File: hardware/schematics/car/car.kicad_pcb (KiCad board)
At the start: 12 copper layers, 17.9 x 30.1 mm, 19 parts, among them M1 Motor_Servo, Q1 PMOS, SW2 SW_Push, SW3 SW_Push, U1 VL53L0CXV0DH1, U10 Mini-560, U11 JGA25-37x, U2 VL53L0CXV0DH1, U3 VL53L0CXV0DH1, U4 Pixy2, U6 TB6612FNG, U7 SparkFun OTOS, U9 Mini-360

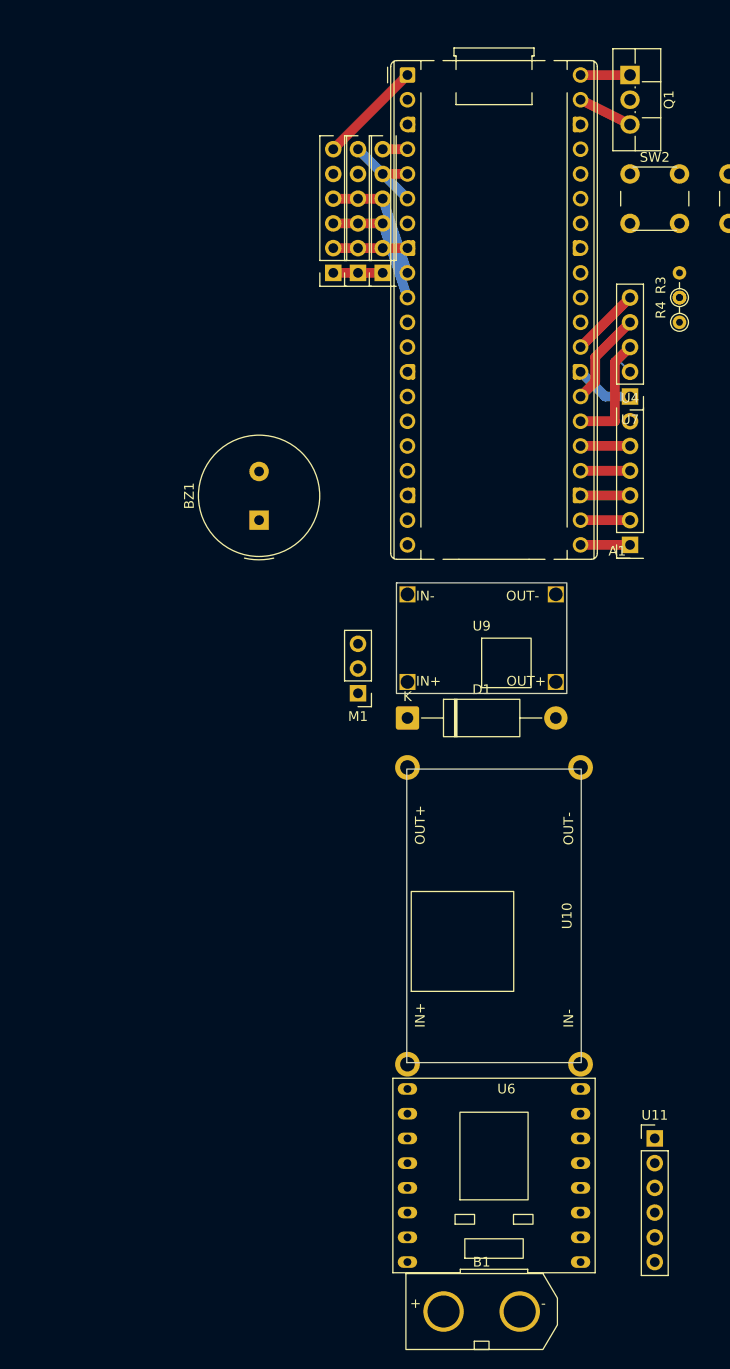
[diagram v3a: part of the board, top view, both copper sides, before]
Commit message: [Schematic] Fix mini560 footprint. PCB: some moving.
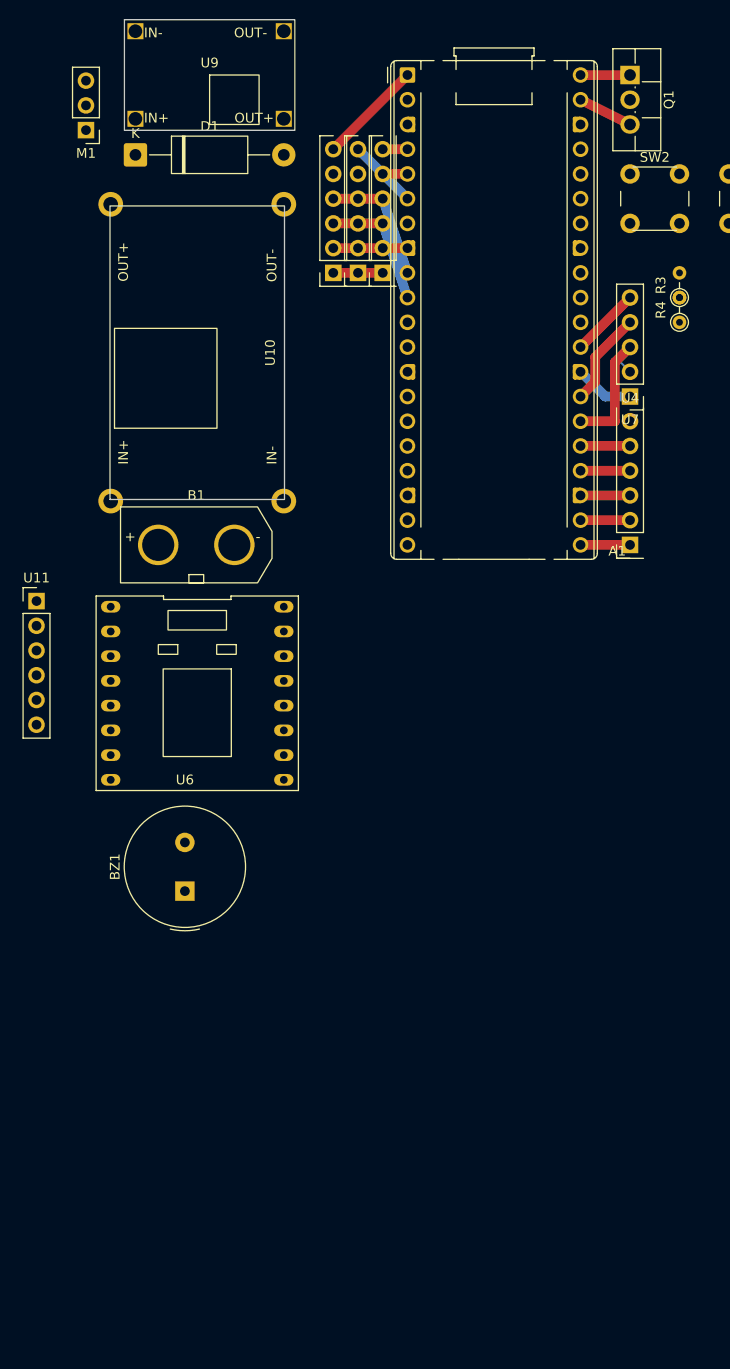
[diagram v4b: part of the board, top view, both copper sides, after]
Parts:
- moved U11 84.1 mm to (88.9, 69.3)
- moved B1 84.0 mm to (105.3, 63.5)
- moved U10 65.4 mm to (105.4, 43.8)
- moved D1 64.2 mm to (99.1, 23.4)
- moved M1 64.2 mm to (94.0, 20.9)
- moved U9 64.2 mm to (106.7, 15.2)
- moved U6 58.2 mm to (105.4, 78.7), turned to -90 degrees
- moved BZ1 38.9 mm to (104.1, 99.1)
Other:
- board size 17.9 x 30.1 mm -> 17.9 x 30.2 mm
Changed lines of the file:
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@@
 	(footprint "xlnc-foot:Buck_Mini-560_2.54mm"
 		(layer "F.Cu")
-		(at 135.89 101.6 90)
+		(at 105.41 43.76 90)
 		(property "Reference" "U10"
 			(at 0 7.5 90)
@@
 		(sheetname "/")
 		(sheetfile "car.kicad_sch")
-		(units
-			(unit
-				(name "A")
-				(pins "1" "2" "3" "4")
-			)
-		)
 		(attr smd)
 		(duplicate_pad_numbers_are_jumpers no)
@@
 		)
 		(pad "3" thru_hole circle
-			(at 15.24 -8.89 90)
+			(at 15.24 8.89 90)
 			(size 2.54 2.54)
 			(drill 1.5)
@@
 		)
 		(pad "4" thru_hole circle
-			(at 15.24 8.89 90)
+			(at 15.24 -8.89 90)
 			(size 2.54 2.54)
 			(drill 1.5)
@@
 	(footprint "xlnc-foot:TB6612FNG_Breakout_Sparkfun"
 		(layer "F.Cu")
-		(at 135.89 128.27 90)
+		(at 105.41 78.74 -90)
 		(tags "TB6612FNG, driver motor")
 		(property "Reference" "U6"
@@
 		(duplicate_pad_numbers_are_jumpers no)
 		(fp_line
-			(start 9.99 -10.39)
-			(end -9.99 -10.39)
+			(start -9.99 10.39)
+			(end 9.99 10.39)
 			(stroke
 				(width 0.12)
@@
 		)
 		(fp_line
-			(start -9.99 -10.39)
-			(end -9.99 -3.463333)
+			(start 9.99 10.39)
+			(end 9.99 -10.39)
 			(stroke
 				(width 0.12)
@@
 		)
 		(fp_line
-			(start -9.63 -3.463333)
-			(end -9.63 3.463333)
+			(start -9.99 3.463333)
+			(end -9.99 10.39)
 			(stroke
 				(width 0.12)
@@
 		)
 		(fp_line
-			(start -9.99 -3.463333)
-			(end -9.63 -3.463333)
+			(start -9.63 3.463333)
+			(end -9.99 3.463333)
 			(stroke
 				(width 0.12)
@@
 		)
 		(fp_line
-			(start -9.63 3.463333)
-			(end -9.99 3.463333)
+			(start -9.99 -3.463333)
+			(end -9.63 -3.463333)
 			(stroke
 				(width 0.12)
@@
 		)
 		(fp_line
-			(start -9.99 3.463333)
-			(end -9.99 10.39)
+			(start -9.63 -3.463333)
+			(end -9.63 3.463333)
 			(stroke
 				(width 0.12)
@@
 		)
 		(fp_line
-			(start 9.99 10.39)
-			(end 9.99 -10.39)
+			(start -9.99 -10.39)
+			(end -9.99 -3.463333)
 			(stroke
 				(width 0.12)
@@
 		)
 		(fp_line
-			(start -9.99 10.39)
-			(end 9.99 10.39)
+			(start 9.99 -10.39)
+			(end -9.99 -10.39)
 			(stroke
 				(width 0.12)
@@
 		)
 		(fp_rect
-			(start -5 -4)
-			(end -4 -2)
+			(start -5 2)
+			(end -4 4)
 			(stroke
 				(width 0.1)
@@
 		)
 		(fp_rect
-			(start -2.5 -3.5)
-			(end 6.5 3.5)
+			(start -8.5 -3)
+			(end -6.5 3)
 			(stroke
 				(width 0.1)
@@
 		)
 		(fp_rect
-			(start -8.5 -3)
-			(end -6.5 3)
+			(start -2.5 -3.5)
+			(end 6.5 3.5)
 			(stroke
 				(width 0.1)
@@
 		)
 		(fp_rect
-			(start -5 2)
-			(end -4 4)
+			(start -5 -4)
+			(end -4 -2)
 			(stroke
 				(width 0.1)
@@
 		)
 		(fp_line
-			(start 9.74 -10.14)
-			(end 9.74 10.14)
+			(start -9.74 10.14)
+			(end -9.74 -10.14)
 			(stroke
 				(width 0.05)
@@
 		)
 		(fp_line
-			(start -9.74 -10.14)
-			(end 9.74 -10.14)
+			(start 9.74 10.14)
+			(end -9.74 10.14)
 			(stroke
 				(width 0.05)
@@
 		)
 		(fp_line
-			(start 9.74 10.14)
-			(end -9.74 10.14)
+			(start -9.74 -10.14)
+			(end 9.74 -10.14)
 			(stroke
 				(width 0.05)
@@
 		)
 		(fp_line
-			(start -9.74 10.14)
-			(end -9.74 -10.14)
+			(start 9.74 -10.14)
+			(end 9.74 10.14)
 			(stroke
 				(width 0.05)
@@
 		)
 		(pad "1" thru_hole oval
-			(at -1.27 8.89 90)
+			(at -1.27 8.89 270)
 			(size 1.2 2)
 			(drill 0.8)
@@
 		)
 		(pad "5" thru_hole oval
-			(at 1.27 8.89 90)
+			(at 1.27 8.89 270)
 			(size 1.2 2)
 			(drill 0.8)
@@
 		)
 		(pad "7" thru_hole oval
-			(at 3.81 8.89 90)
+			(at 3.81 8.89 270)
 			(size 1.2 2)
 			(drill 0.8)
@@
 		)
 		(pad "11" thru_hole oval
-			(at 6.35 8.89 90)
+			(at 6.35 8.89 270)
 			(size 1.2 2)
 			(drill 0.8)
@@
 		)
 		(pad "15" thru_hole oval
-			(at 6.35 -8.89 90)
+			(at 6.35 -8.89 270)
 			(size 1.2 2)
 			(drill 0.8)
@@
 		)
 		(pad "16" thru_hole oval
-			(at 3.81 -8.89 90)
+			(at 3.81 -8.89 270)
 			(size 1.2 2)
 			(drill 0.8)
@@
 		)
 		(pad "17" thru_hole oval
-			(at 1.27 -8.89 90)
+			(at 1.27 -8.89 270)
 			(size 1.2 2)
 			(drill 0.8)
@@
 		)
 		(pad "18" thru_hole oval
-			(at -3.81 8.89 90)
+			(at -3.81 8.89 270)
 			(size 1.2 2)
 			(drill 0.8)
@@
 		)
 		(pad "18" thru_hole oval
-			(at 8.89 -8.89 90)
+			(at 8.89 -8.89 270)
 			(size 1.2 2)
 			(drill 0.8)
@@
 		)
 		(pad "18" thru_hole oval
-			(at 8.89 8.89 90)
+			(at 8.89 8.89 270)
 			(size 1.2 2)
 			(drill 0.8)
@@
 		)
 		(pad "19" thru_hole oval
-			(at -1.27 -8.89 90)
+			(at -1.27 -8.89 270)
 			(size 1.2 2)
 			(drill 0.8)
@@
 		)
 		(pad "20" thru_hole oval
-			(at -6.35 8.89 90)
+			(at -6.35 8.89 270)
 			(size 1.2 2)
 			(drill 0.8)
@@
 		)
 		(pad "21" thru_hole oval
-			(at -3.81 -8.89 90)
+			(at -3.81 -8.89 270)
 			(size 1.2 2)
 			(drill 0.8)
@@
 		)
 		(pad "22" thru_hole oval
-			(at -6.35 -8.89 90)
+			(at -6.35 -8.89 270)
 			(size 1.2 2)
 			(drill 0.8)
@@
 		)
 		(pad "23" thru_hole oval
-			(at -8.89 -8.89 90)
+			(at -8.89 -8.89 270)
 			(size 1.2 2)
 			(drill 0.8)
@@
 		)
 		(pad "24" thru_hole oval
-			(at -8.89 8.89 90)
+			(at -8.89 8.89 270)
 			(size 1.2 2)
 			(drill 0.8)
@@
 	(footprint "xlnc-foot:Buck_Mini-360"
 		(layer "F.Cu")
-		(at 134.62 73.08)
+		(at 106.68 15.24)
 		(property "Reference" "U9"
 			(at 0 -1.25 0)
@@
 	(footprint "Diode_THT:D_DO-15_P15.24mm_Horizontal"
 		(layer "F.Cu")
-		(at 127 81.28)
+		(at 99.06 23.44)
 		(descr "Diode, DO-15 series, Axial, Horizontal, pin pitch=15.24mm, length*diameter=7.6*3.6mm^2, http://www.diodes.com/_files/packages/DO-15.pdf")
 		(tags "Diode DO-15 series Axial Horizontal pin pitch 15.24mm  length 7.6mm diameter 3.6mm")
@@
 	(footprint "xlnc-foot:XT60"
 		(layer "F.Cu")
-		(at 134.62 142.24)
+		(at 105.31 63.5)
 		(property "Reference" "B1"
 			(at 0 -5.08 0)
@@
 	(footprint "Buzzer_Beeper:Buzzer_TDK_PS1240P02BT_D12.2mm_H6.5mm"
 		(layer "F.Cu")
-		(at 111.76 60.96 90)
+		(at 104.14 99.06 90)
 		(descr "Buzzer, D12.2mm height 6.5mm, https://product.tdk.com/info/en/catalog/datasheets/piezoelectronic_buzzer_ps_en.pdf")
 		(tags "buzzer")
@@
 	(footprint "Connector_PinHeader_2.54mm:PinHeader_1x03_P2.54mm_Vertical"
 		(layer "F.Cu")
-		(at 121.92 78.74 180)
+		(at 93.98 20.9 180)
 		(descr "Through hole straight pin header, 1x03, 2.54mm pitch, single row")
 		(tags "Through hole pin header THT 1x03 2.54mm single row")
@@
 	(footprint "Connector_PinHeader_2.54mm:PinHeader_1x06_P2.54mm_Vertical"
 		(layer "F.Cu")
-		(at 152.4 124.46)
+		(at 88.9 69.27)
 		(descr "Through hole straight pin header, 1x06, 2.54mm pitch, single row")
 		(tags "Through hole pin header THT 1x06 2.54mm single row")

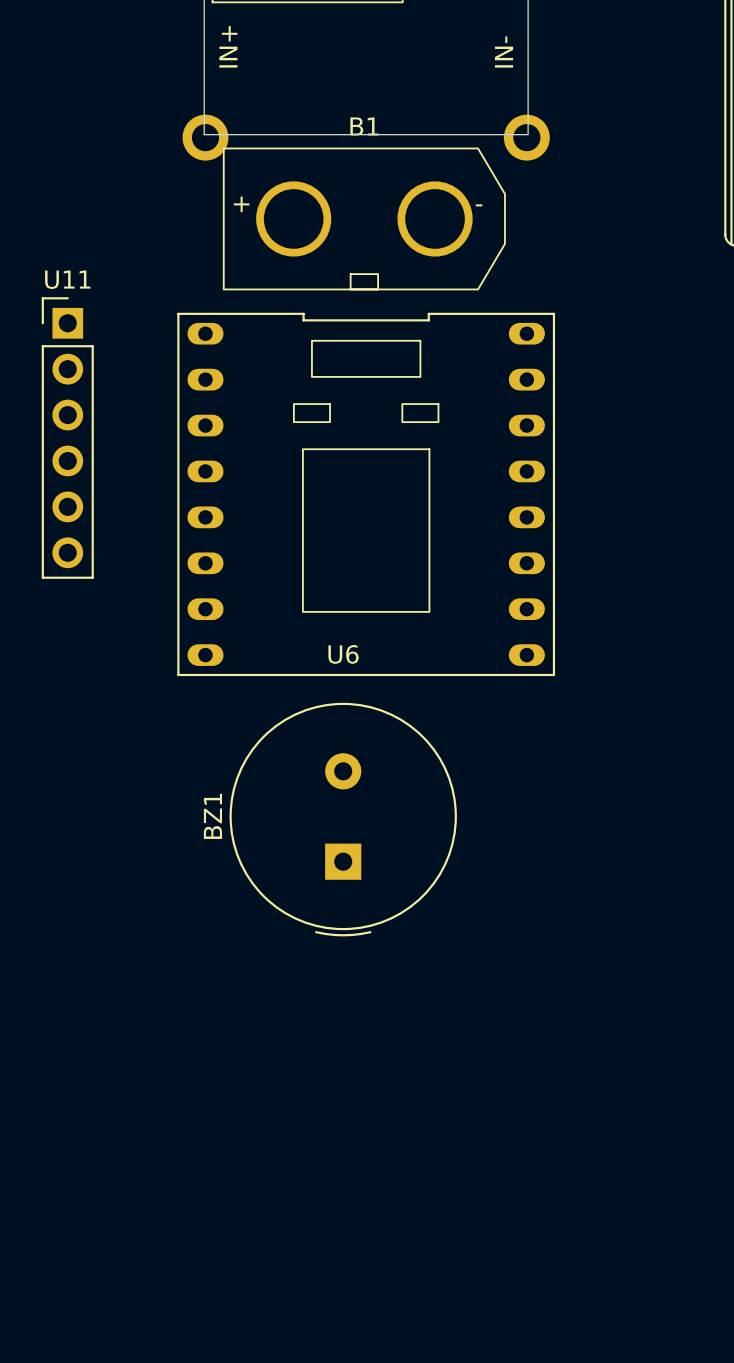
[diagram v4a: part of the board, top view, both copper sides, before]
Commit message: [Schematic] Add battery switch to pcb.
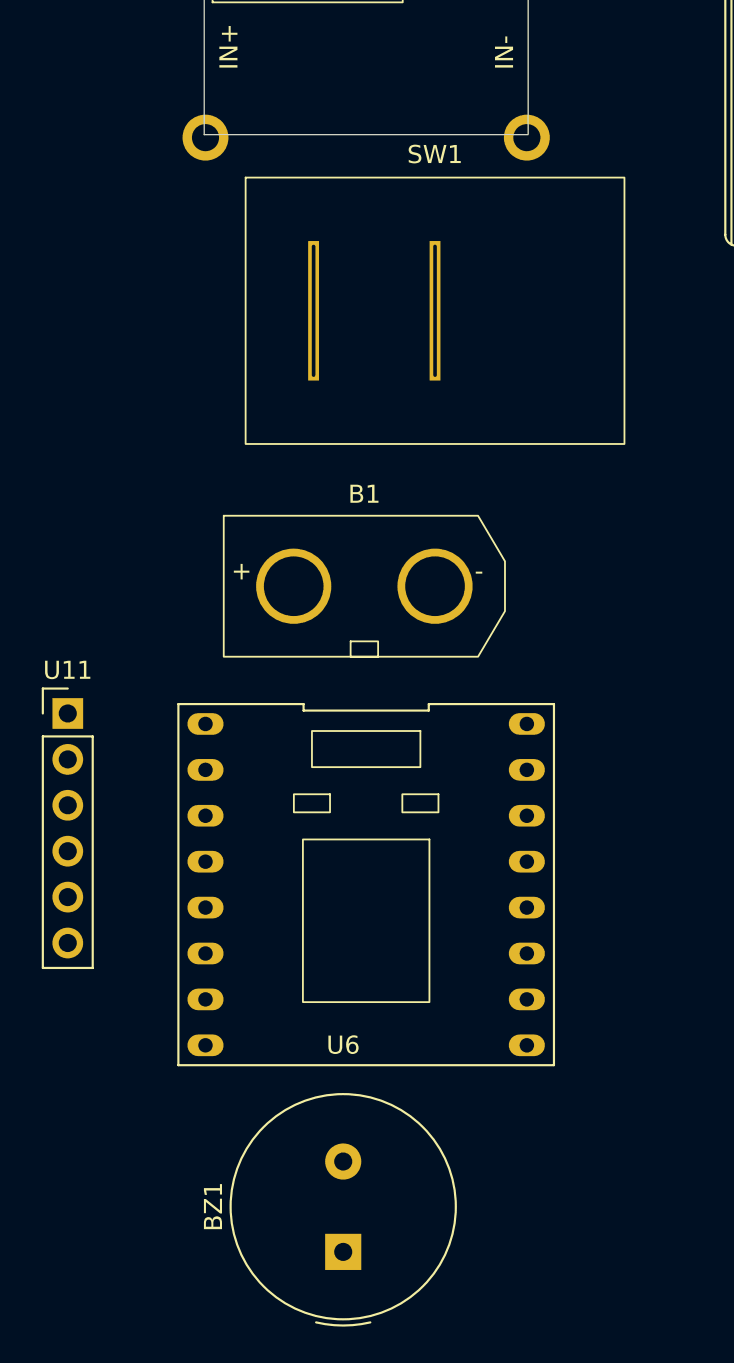
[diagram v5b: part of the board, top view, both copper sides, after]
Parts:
- added SW1: SW_SPST, xlnc-foot:SW_SPST_20.96mmx14.74mm, F.Cu at (109.2, 68.6)
- moved BZ1 21.6 mm to (104.1, 120.7)
- moved U11 21.6 mm to (88.9, 90.9)
- moved U6 21.6 mm to (105.4, 100.3)
- moved B1 20.3 mm to (105.3, 83.8)
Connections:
- B1 pad 1: VBAT -> Net-(B1-+)
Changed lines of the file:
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@@
 		(sheetname "/")
 		(sheetfile "car.kicad_sch")
+		(units
+			(unit
+				(name "A")
+				(pins "1" "2" "3" "4")
+			)
+		)
 		(attr smd)
 		(duplicate_pad_numbers_are_jumpers no)
@@
 		(embedded_fonts no)
 	)
+	(footprint "xlnc-foot:SW_SPST_20.96mmx14.74mm"
+		(layer "F.Cu")
+		(at 109.22 68.58)
+		(property "Reference" "SW1"
+			(at 0 -8.636 0)
+			(unlocked yes)
+			(layer "F.SilkS")
+			(effects
+				(font
+					(size 1 1)
+					(thickness 0.1)
+				)
+			)
+		)
+		(property "Value" "SW_SPST"
+			(at 0 8.89 0)
+			(unlocked yes)
+			(layer "F.Fab")
+			(effects
+				(font
+					(size 1 1)
+					(thickness 0.15)
+				)
+			)
+		)
+		(property "Datasheet" ""
+			(at 0 0 0)
+			(unlocked yes)
+			(layer "F.Fab")
+			(hide yes)
+			(effects
+				(font
+					(size 1 1)
+					(thickness 0.15)
+				)
+			)
+		)
+		(property "Description" "Single Pole Single Throw (SPST) switch"
+			(at 0 0 0)
+			(unlocked yes)
+			(layer "F.Fab")
+			(hide yes)
+			(effects
+				(font
+					(size 1 1)
+					(thickness 0.15)
+				)
+			)
+		)
+		(sheetname "/")
+		(sheetfile "car.kicad_sch")
+		(units
+			(unit
+				(name "A")
+				(pins "1" "2")
+			)
+		)
+		(attr smd)
+		(duplicate_pad_numbers_are_jumpers no)
+		(fp_rect
+			(start -10.48 -7.37)
+			(end 10.48 7.37)
+			(stroke
+				(width 0.1)
+				(type solid)
+			)
+			(fill no)
+			(layer "F.SilkS")
+		)
+		(fp_text user "${REFERENCE}"
+			(at 0 10.414 0)
+			(unlocked yes)
+			(layer "F.Fab")
+			(effects
+				(font
+					(size 1 1)
+					(thickness 0.15)
+				)
+			)
+		)
+		(pad "1" thru_hole rect
+			(at -6.72 0)
+			(size 0.6 7.72)
+			(drill oval 0.2 7.32)
+			(layers "*.Cu" "*.Mask")
+			(remove_unused_layers no)
+			(net "Net-(B1-+)")
+			(pinfunction "A_1")
+			(pintype "passive")
+		)
+		(pad "2" thru_hole rect
+			(at 0 0)
+			(size 0.6 7.72)
+			(drill oval 0.2 7.32)
+			(layers "*.Cu" "*.Mask")
+			(remove_unused_layers no)
+			(net "VBAT")
+			(pinfunction "B_2")
+			(pintype "passive")
+		)
+		(embedded_fonts no)
+	)
 	(footprint "xlnc-foot:TB6612FNG_Breakout_Sparkfun"
 		(layer "F.Cu")
-		(at 105.41 78.74 -90)
+		(at 105.41 100.33 -90)
 		(tags "TB6612FNG, driver motor")
 		(property "Reference" "U6"
@@
 	(footprint "xlnc-foot:XT60"
 		(layer "F.Cu")
-		(at 105.31 63.5)
+		(at 105.31 83.82)
 		(property "Reference" "B1"
 			(at 0 -5.08 0)
@@
 			(layers "*.Cu" "*.Mask")
 			(remove_unused_layers no)
-			(net "VBAT")
+			(net "Net-(B1-+)")
 			(pinfunction "+_1")
 			(pintype "power_out")
@@
 	(footprint "Buzzer_Beeper:Buzzer_TDK_PS1240P02BT_D12.2mm_H6.5mm"
 		(layer "F.Cu")
-		(at 104.14 99.06 90)
+		(at 104.14 120.65 90)
 		(descr "Buzzer, D12.2mm height 6.5mm, https://product.tdk.com/info/en/catalog/datasheets/piezoelectronic_buzzer_ps_en.pdf")
 		(tags "buzzer")
@@
 	(footprint "Connector_PinHeader_2.54mm:PinHeader_1x06_P2.54mm_Vertical"
 		(layer "F.Cu")
-		(at 88.9 69.27)
+		(at 88.9 90.86)
 		(descr "Through hole straight pin header, 1x06, 2.54mm pitch, single row")
 		(tags "Through hole pin header THT 1x06 2.54mm single row")

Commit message: [Schematic] pcb movings.
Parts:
- moved BZ1 100.6 mm to (165.1, 40.6)
- moved D1 85.0 mm to (129.5, 102.8)
- moved U9 85.0 mm to (137.2, 94.6)
- moved M1 85.0 mm to (124.5, 100.2)
- moved B1 62.9 mm to (167.6, 92.6), turned to -90 degrees
- moved U10 60.9 mm to (163.8, 61.0)
- moved SW1 51.7 mm to (154.9, 92.6), turned to -90 degrees
- moved U11 38.5 mm to (121.9, 71.1)
- moved U6 38.1 mm to (135.9, 77.5)
- moved SW2 16.3 mm to (165.1, 17.8), turned to -90 degrees
- moved SW3 11.4 mm to (157.5, 17.8), turned to 90 degrees
- moved R3 9.16 mm to (149.9, 30.5)
- moved R4 9.16 mm to (149.9, 33.0)
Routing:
- net GND: track 18.8 -> 57.5 mm
- net Net-(A1-GPIO27_ADC1): track 0.00 -> 34.1 mm
- net Net-(A1-GPIO28_ADC2): track 0.00 -> 19.4 mm
- net Net-(A1-GPIO26_ADC0): track 0.00 -> 9.16 mm
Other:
- board size 17.9 x 30.2 mm -> 17.9 x 30.1 mm

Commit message: [Schematic] PCB many things
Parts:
- U1, U2, U3: footprint xlnc-foot:VL53L0/1XV2_PinHeader_1x06_P2.54mm_Vertical -> xlnc-foot:VL53L0_1XV2_PinHeader_1x06_P2.54mm_Vertical
- U7: footprint Connector_PinHeader_2.54mm:PinHeader_1x05_P2.54mm_Vertical -> xlnc-foot:Sparkfun_OTOS_PinHeader_1x05_P2.54mm_Vertical
- moved SW2 68.6 mm to (121.9, 71.1), turned to 90 degrees
- moved U11 53.5 mm to (175.3, 74.9), turned to 180 degrees
- moved U4 29.6 mm to (124.5, 66.0), turned to 180 degrees
- moved U7 27.4 mm to (124.5, 38.1), turned to 0 degrees
- moved M1 25.5 mm to (147.3, 88.9)
- moved B1 25.4 mm to (160.0, 116.8), turned to 180 degrees
- moved U6 25.0 mm to (158.8, 67.3), turned to 90 degrees
- moved D1 24.5 mm to (152.4, 94.0)
- moved U9 24.5 mm to (160.0, 85.8)
- moved U10 20.9 mm to (158.8, 40.6)
- moved BZ1 20.5 mm to (167.6, 20.3)
- moved SW1 11.8 mm to (157.5, 104.1), turned to 180 degrees
- moved R3 7.84 mm to (148.0, 38.1), turned to -90 degrees
- moved R4 3.14 mm to (148.0, 35.6), turned to -90 degrees
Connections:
- BZ1 pad 1: Net-(A1-GPIO14) -> Net-(A1-GPIO27_ADC1)
- M1 pad 1: Net-(A1-GPIO15) -> Net-(A1-GPIO22)
- SW2 pad 1: Net-(A1-GPIO27_ADC1) -> Net-(A1-GPIO11)
- U11 pad 3: Net-(A1-GPIO8) -> Net-(A1-GPIO20)
- U11 pad 4: Net-(A1-GPIO9) -> Net-(A1-GPIO21)
- U4 pad 1: Net-(A1-GPIO16) -> Net-(A1-GPIO12)
- U4 pad 3: Net-(A1-GPIO18) -> Net-(A1-GPIO14)
- U4 pad 4: Net-(A1-GPIO19) -> Net-(A1-GPIO15)
- U4 pad 7: Net-(A1-GPIO17) -> Net-(A1-GPIO13)
- U6 pad 19: Net-(A1-GPIO10) -> Net-(A1-GPIO16)
- U6 pad 21: Net-(A1-GPIO11) -> Net-(A1-GPIO18)
- U6 pad 22: Net-(A1-GPIO12) -> Net-(A1-GPIO19)
- U6 pad 23: Net-(A1-GPIO13) -> Net-(A1-GPIO17)
- U7 pad 3: Net-(A1-GPIO20) -> Net-(A1-GPIO8)
- U7 pad 4: Net-(A1-GPIO21) -> Net-(A1-GPIO9)
- U7 pad 5: Net-(A1-GPIO22) -> Net-(A1-GPIO10)
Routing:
- net GND: track 57.5 -> 234.2 mm
- net Net-(A1-GPIO27_ADC1): track 34.1 -> 0.00 mm
- net Net-(A1-GPIO11): track 0.00 -> 30.5 mm
- net +3.3V: track 60.0 -> 83.7 mm
- net Net-(A1-GPIO28_ADC2): track 19.4 -> 0.00 mm
- net Net-(B1-+): track 0.00 -> 12.8 mm
- net Net-(A1-GPIO20): track 11.8 -> 0.00 mm
- net Net-(A1-GPIO21): track 9.72 -> 0.00 mm
- net Net-(A1-GPIO26_ADC0): track 9.16 -> 0.00 mm
- net Net-(A1-GPIO22): track 7.18 -> 0.00 mm
- net Net-(A1-GPIO19): track 5.08 -> 0.00 mm
- net Net-(A1-GPIO18): track 5.08 -> 0.00 mm
- net Net-(A1-GPIO17): track 5.08 -> 0.00 mm
- net Net-(A1-GPIO16): track 5.08 -> 0.00 mm
- net Net-(A1-GPIO9): track 0.00 -> 2.54 mm
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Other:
- board size 17.9 x 30.1 mm -> 17.9 x 30.2 mm
